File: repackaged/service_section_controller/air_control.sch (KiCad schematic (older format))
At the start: 18 parts

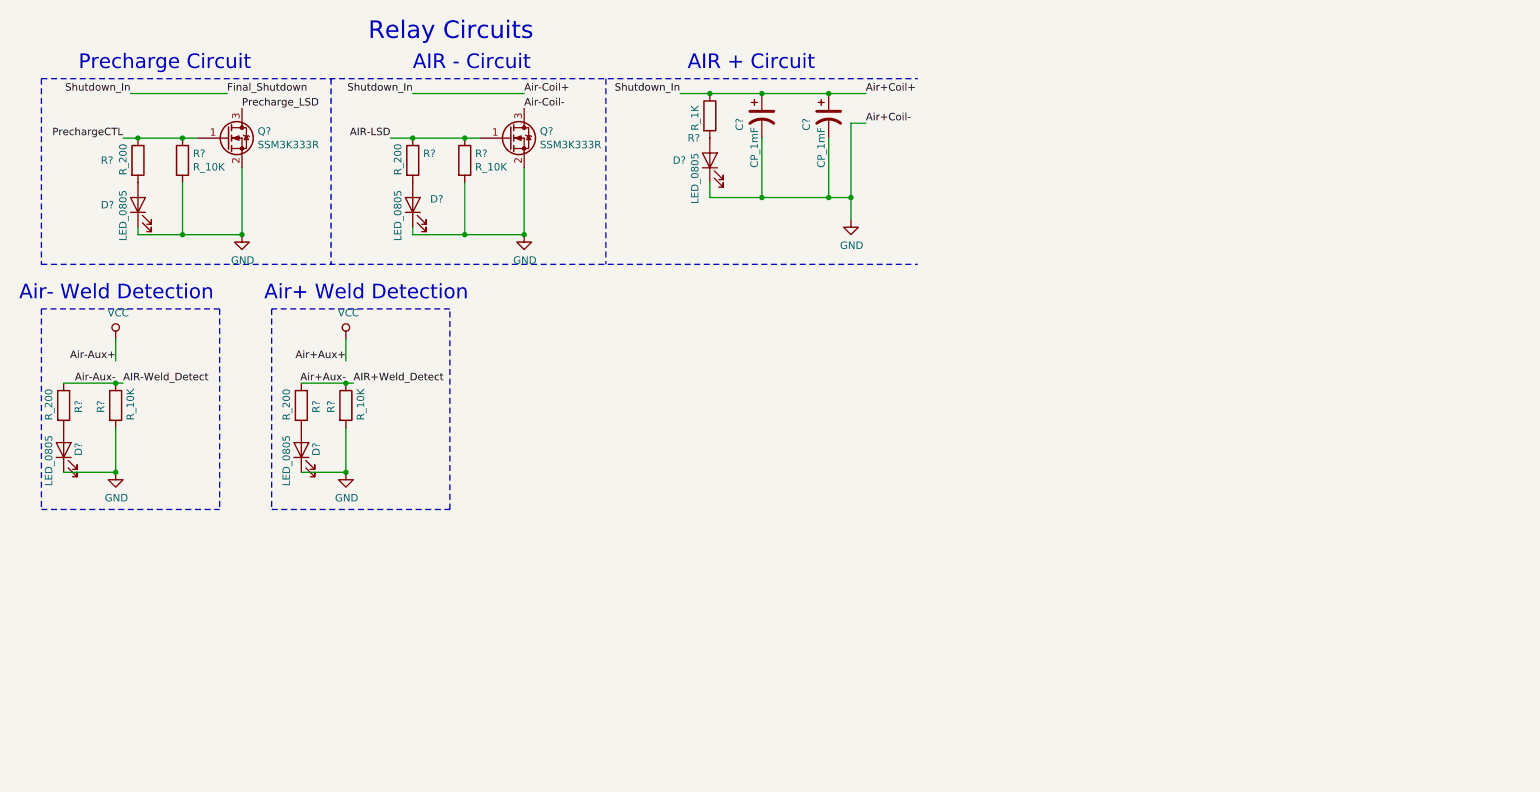
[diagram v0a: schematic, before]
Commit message: changed labels to global and added lin reg
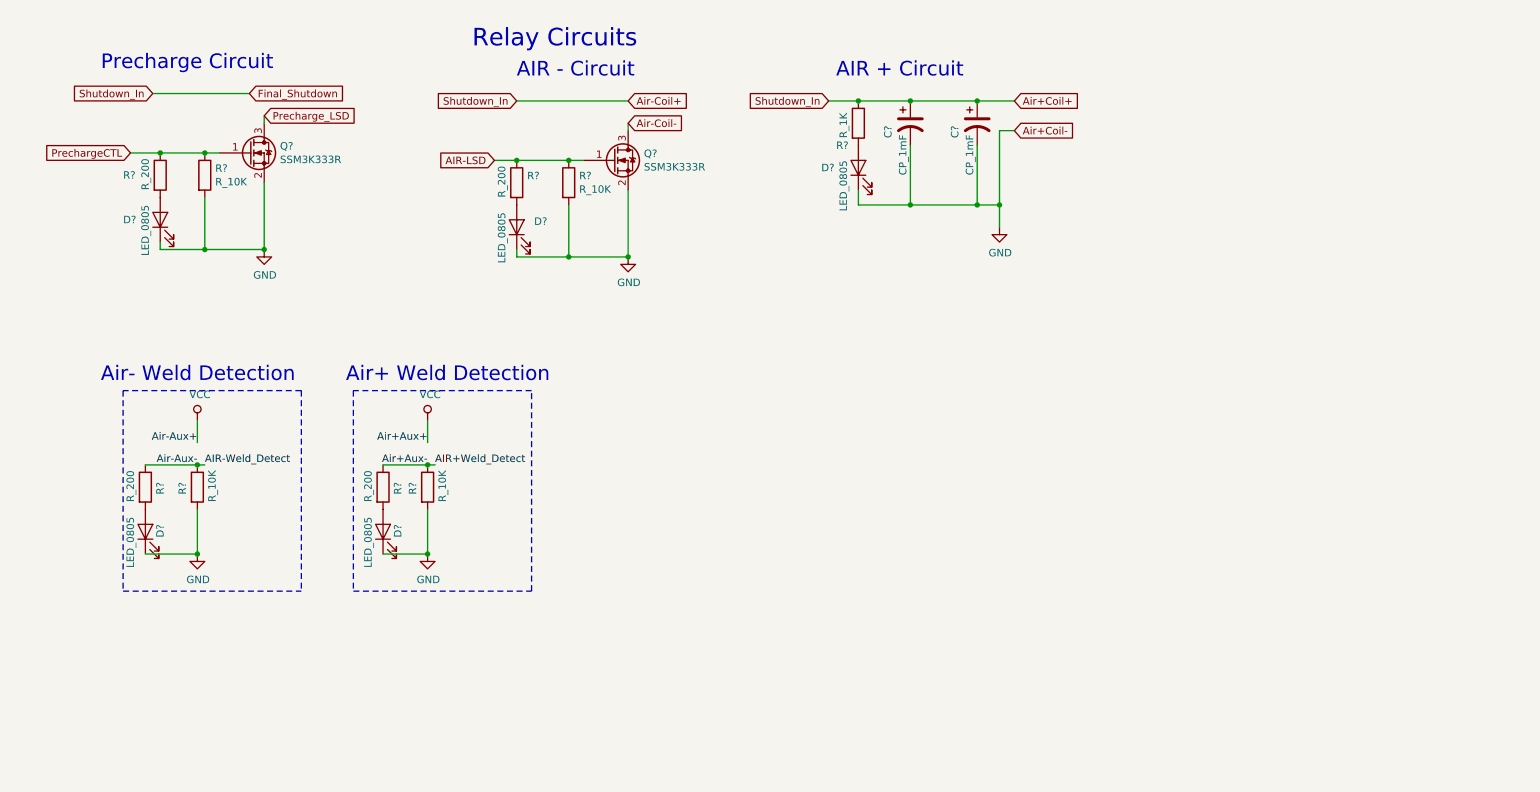
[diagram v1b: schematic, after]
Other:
- moved on the sheet: C?, D?, Q?, R?

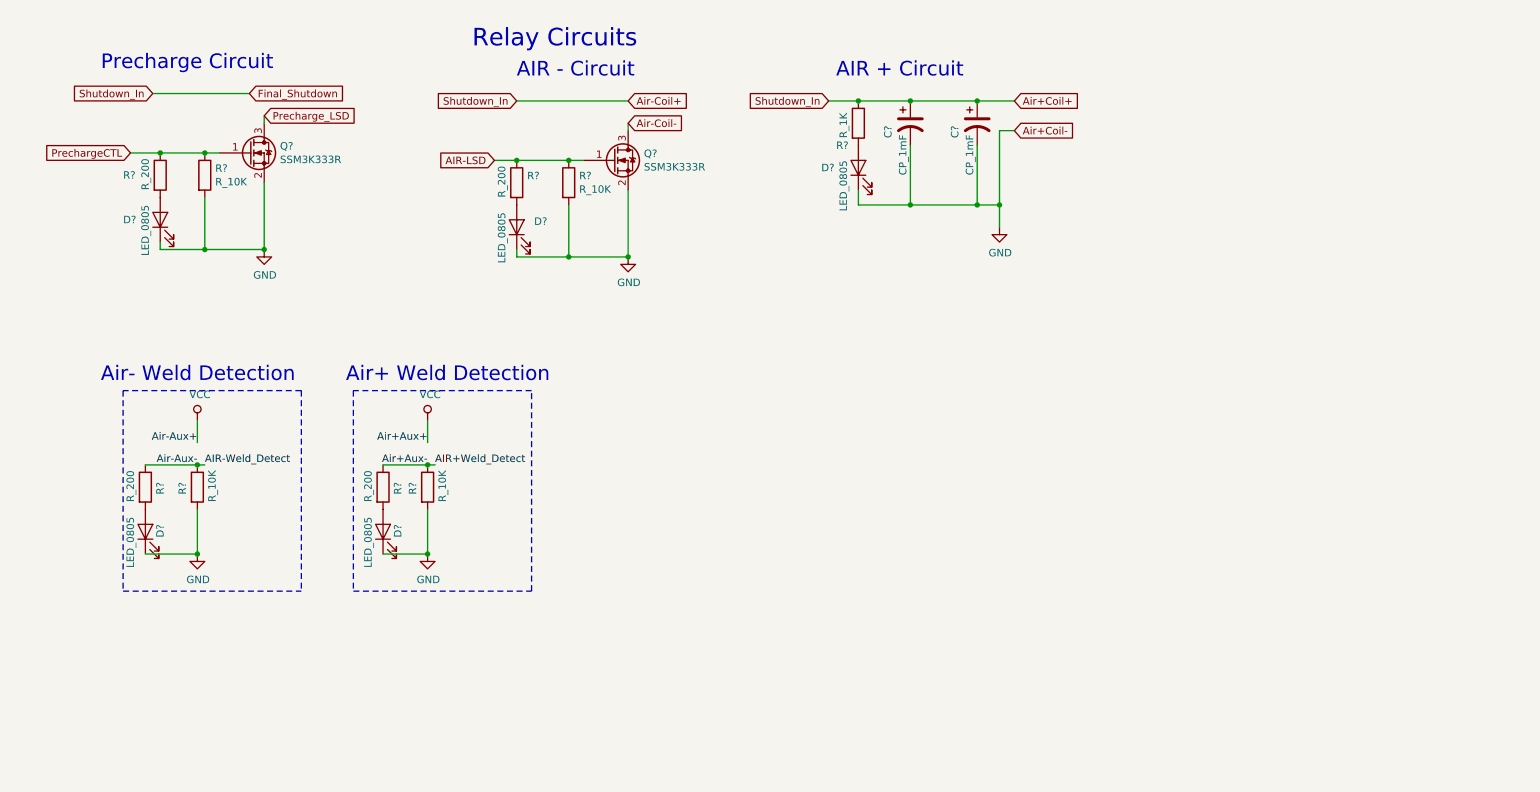
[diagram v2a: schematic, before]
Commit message: modify net labels for LSD circuits
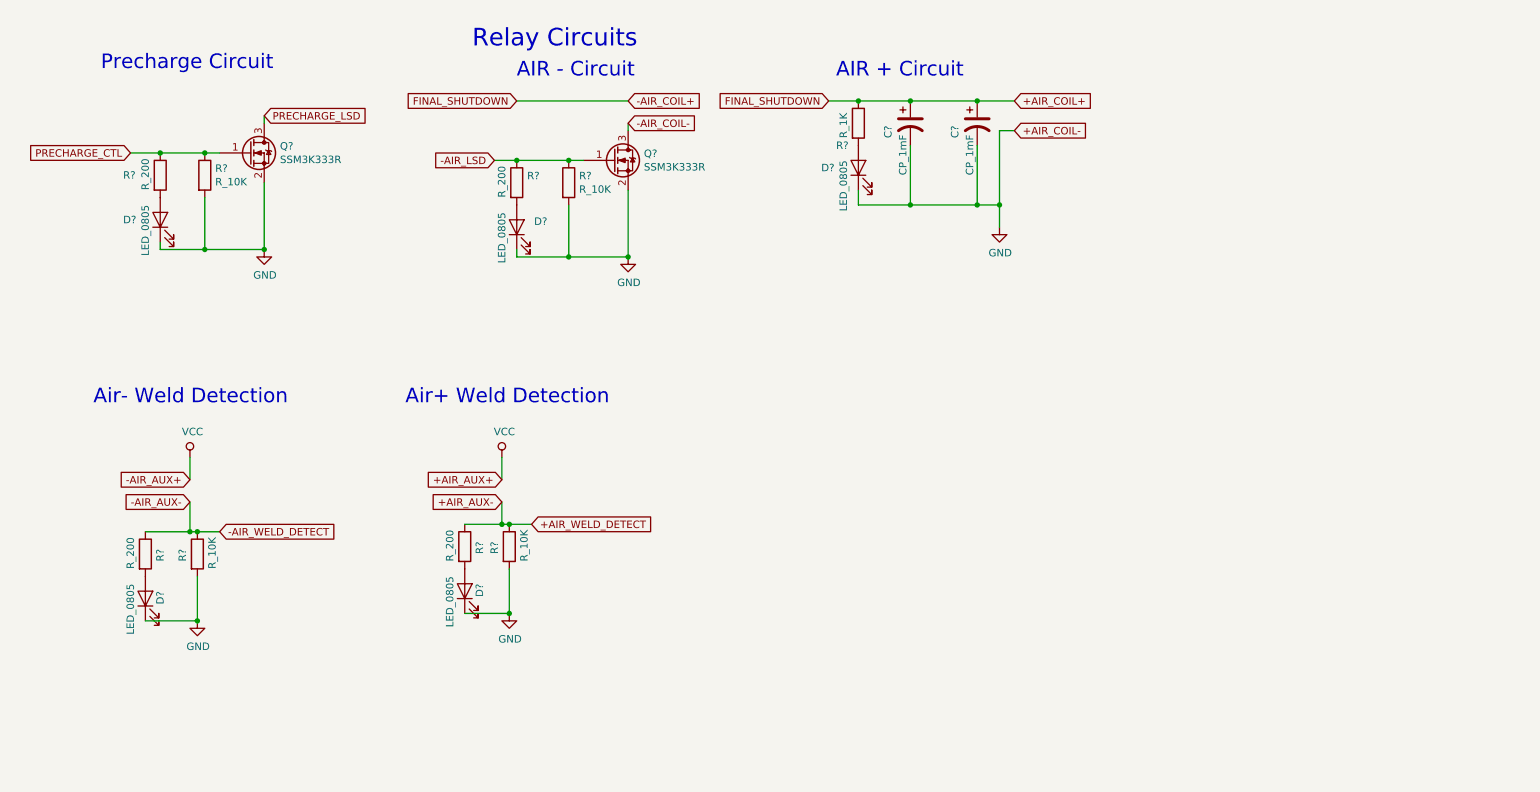
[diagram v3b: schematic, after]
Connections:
- net AIR+Weld_Detect renamed +AIR_AUX-
- net AIR-LSD renamed -AIR_LSD
- net AIR-Weld_Detect renamed -AIR_AUX-
- net Air+Coil+ renamed +AIR_COIL+
- net Air-Coil- renamed -AIR_COIL-
- net PrechargeCTL renamed PRECHARGE_CTL
- net Precharge_LSD renamed PRECHARGE_LSD
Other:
- moved on the sheet: D?, R?

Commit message: changed labels and power nets and added fusing
changed relevant labels to global labels and checked that the
naming is correct. Changed vcc nets to corresponding 5v or 12v.
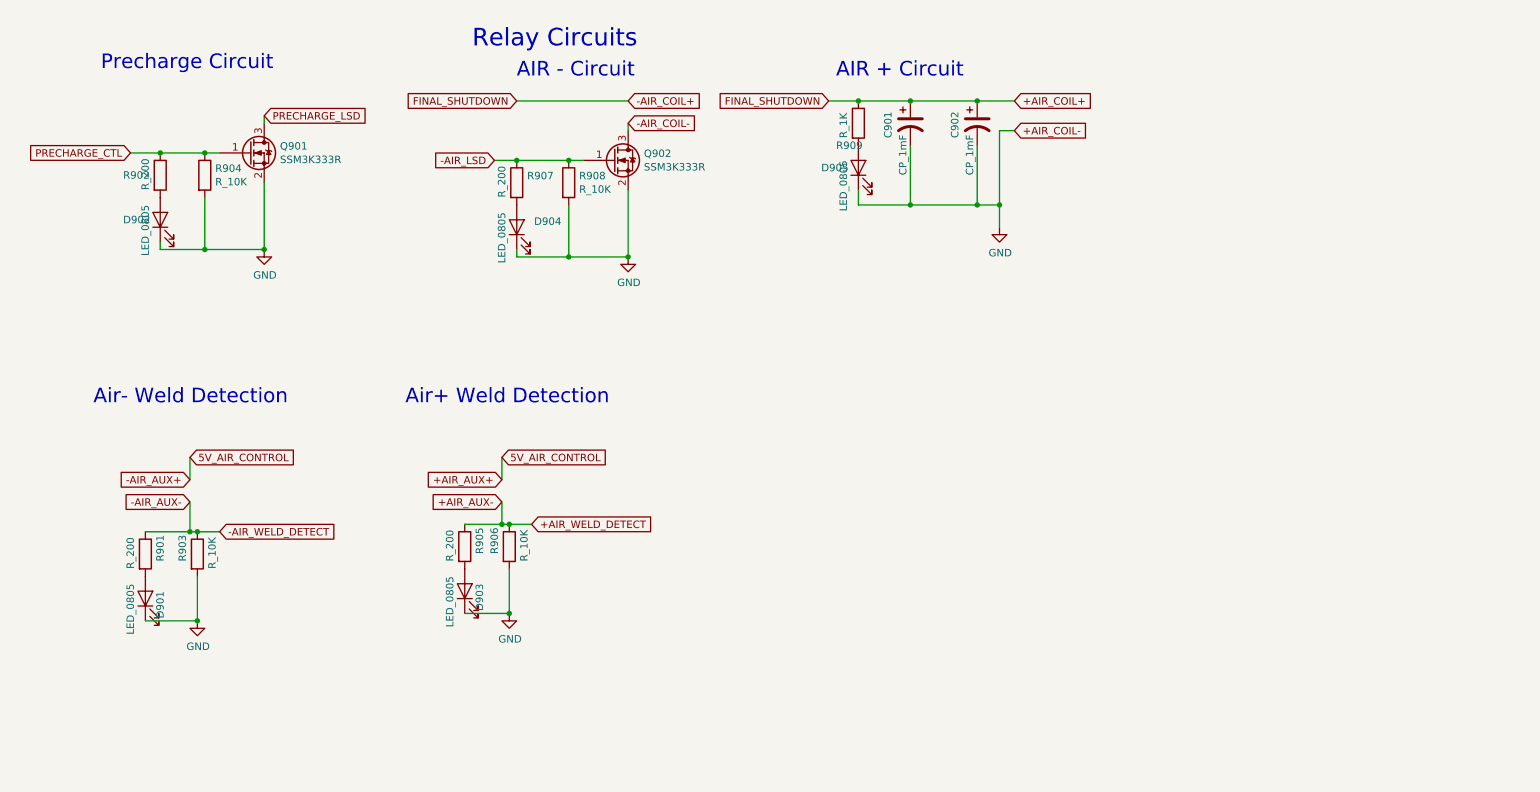
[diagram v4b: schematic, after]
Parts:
- gave numbers to parts that had none: 18
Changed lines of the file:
@@
 $EndComp
 $Comp
-L formula:R_10K R?
+L formula:R_10K R906
 U 1 1 61065F72
 P 4000 4200
-F 0 "R?" V 3900 4150 50  0000 L CNN
+F 0 "R906" V 3900 4150 50  0000 L CNN
 F 1 "R_10K" V 4100 4100 50  0000 L CNN
 F 2 "footprints:R_0805_OEM" H 3930 4200 50  0001 C CNN
@@
 $EndComp
 $Comp
-L formula:LED_0805 D?
+L formula:LED_0805 D903
 U 1 1 61065F7B
 P 3700 4500
-F 0 "D?" H 3750 4400 50  0000 R CNN
+F 0 "D903" H 3750 4400 50  0000 R CNN
 F 1 "LED_0805" H 3800 4600 50  0000 R CNN
 F 2 "footprints:LED_0805_OEM" H 3600 4500 50  0001 C CNN
@@
 $EndComp
 $Comp
-L formula:R_200 R?
+L formula:R_200 R905
 U 1 1 61065F84
 P 3700 4200
-F 0 "R?" V 3800 4150 50  0000 L CNN
+F 0 "R905" V 3800 4150 50  0000 L CNN
 F 1 "R_200" V 3600 4100 50  0000 L CNN
 F 2 "footprints:R_0805_OEM" H 3630 4200 50  0001 C CNN
@@
 Wire Wire Line
 	3950 3600 3950 3750
-$Comp
-L power:VCC #PWR0199
-U 1 1 61065F8F
-P 3950 3600
-F 0 "#PWR0199" H 3950 3450 50  0001 C CNN
-F 1 "VCC" H 3967 3773 50  0000 C CNN
-F 2 "" H 3950 3600 50  0001 C CNN
-F 3 "" H 3950 3600 50  0001 C CNN
-	1    3950 3600
-	1    0    0    -1
-$EndComp
 $Comp
 L power:GND #PWR0200
@@
 	1900 4400 1900 4700
 $Comp
-L formula:LED_0805 D?
+L formula:LED_0805 D901
 U 1 1 61065FA0
 P 1550 4550
-F 0 "D?" H 1600 4450 50  0000 R CNN
+F 0 "D901" H 1600 4450 50  0000 R CNN
 F 1 "LED_0805" H 1650 4650 50  0000 R CNN
 F 2 "footprints:LED_0805_OEM" H 1450 4550 50  0001 C CNN
@@
 	1550 4100 1850 4100
 $Comp
-L formula:R_200 R?
+L formula:R_200 R901
 U 1 1 61065FAA
 P 1550 4250
-F 0 "R?" V 1650 4200 50  0000 L CNN
+F 0 "R901" V 1650 4200 50  0000 L CNN
 F 1 "R_200" V 1450 4150 50  0000 L CNN
 F 2 "footprints:R_0805_OEM" H 1480 4250 50  0001 C CNN
@@
 $EndComp
 $Comp
-L formula:R_10K R?
+L formula:R_10K R903
 U 1 1 61065FB3
 P 1900 4250
-F 0 "R?" V 1800 4200 50  0000 L CNN
+F 0 "R903" V 1800 4200 50  0000 L CNN
 F 1 "R_10K" V 2000 4150 50  0000 L CNN
 F 2 "footprints:R_0805_OEM" H 1830 4250 50  0001 C CNN
@@
 Wire Wire Line
 	1850 3600 1850 3750
-$Comp
-L power:VCC #PWR0201
-U 1 1 61065FBC
-P 1850 3600
-F 0 "#PWR0201" H 1850 3450 50  0001 C CNN
-F 1 "VCC" H 1867 3773 50  0000 C CNN
-F 2 "" H 1850 3600 50  0001 C CNN
-F 3 "" H 1850 3600 50  0001 C CNN
-	1    1850 3600
-	1    0    0    -1
-$EndComp
 Text Notes 3300 3250 0    98   ~ 0
 Air+ Weld Detection
@@
 	4800 1800 4800 2250
 $Comp
-L formula:LED_0805 D?
+L formula:LED_0805 D904
 U 1 1 6106600B
 P 4050 2050
-F 0 "D?" V 4089 1933 50  0000 R CNN
+F 0 "D904" V 4089 1933 50  0000 R CNN
 F 1 "LED_0805" H 4150 2150 50  0000 R CNN
 F 2 "footprints:LED_0805_OEM" H 3950 2050 50  0001 C CNN
@@
 Connection ~ 4400 1600
 $Comp
-L formula:R_10K R?
+L formula:R_10K R908
 U 1 1 61066016
 P 4400 1750
-F 0 "R?" H 4470 1796 50  0000 L CNN
+F 0 "R908" H 4470 1796 50  0000 L CNN
 F 1 "R_10K" H 4470 1705 50  0000 L CNN
 F 2 "footprints:R_0805_OEM" H 4330 1750 50  0001 C CNN
@@
 Connection ~ 4050 1600
 $Comp
-L formula:R_200 R?
+L formula:R_200 R907
 U 1 1 61066021
 P 4050 1750
-F 0 "R?" H 4120 1796 50  0000 L CNN
+F 0 "R907" H 4120 1796 50  0000 L CNN
 F 1 "R_200" V 3950 1650 50  0000 L CNN
 F 2 "footprints:R_0805_OEM" H 3980 1750 50  0001 C CNN
@@
 	4500 1600 4400 1600
 $Comp
-L formula:SSM3K333R Q?
+L formula:SSM3K333R Q902
 U 1 1 6106602C
 P 4700 1600
-F 0 "Q?" H 4906 1646 50  0000 L CNN
+F 0 "Q902" H 4906 1646 50  0000 L CNN
 F 1 "SSM3K333R" H 4906 1555 50  0000 L CNN
 F 2 "footprints:SOT-23F" H 4900 1525 50  0001 L CIN
@@
 Connection ~ 1950 1550
 $Comp
-L formula:R_200 R?
+L formula:R_200 R902
 U 1 1 61066040
 P 1650 1700
-F 0 "R?" H 1400 1700 50  0000 L CNN
+F 0 "R902" H 1400 1700 50  0000 L CNN
 F 1 "R_200" V 1550 1600 50  0000 L CNN
 F 2 "footprints:R_0805_OEM" H 1580 1700 50  0001 C CNN
@@
 $EndComp
 $Comp
-L formula:LED_0805 D?
+L formula:LED_0805 D902
 U 1 1 61066049
 P 1650 2000
-F 0 "D?" V 1650 2250 50  0000 R CNN
+F 0 "D902" V 1650 2250 50  0000 R CNN
 F 1 "LED_0805" H 1750 2100 50  0000 R CNN
 F 2 "footprints:LED_0805_OEM" H 1550 2000 50  0001 C CNN
@@
 	2050 1550 1950 1550
 $Comp
-L formula:SSM3K333R Q?
+L formula:SSM3K333R Q901
 U 1 1 61066054
 P 2250 1550
-F 0 "Q?" H 2456 1596 50  0000 L CNN
+F 0 "Q901" H 2456 1596 50  0000 L CNN
 F 1 "SSM3K333R" H 2456 1505 50  0000 L CNN
 F 2 "footprints:SOT-23F" H 2450 1475 50  0001 L CIN
@@
 Air- Weld Detection
 $Comp
-L formula:R_10K R?
+L formula:R_10K R904
 U 1 1 61066090
 P 1950 1700
-F 0 "R?" H 2020 1746 50  0000 L CNN
+F 0 "R904" H 2020 1746 50  0000 L CNN
 F 1 "R_10K" H 2020 1655 50  0000 L CNN
 F 2 "footprints:R_0805_OEM" H 1880 1700 50  0001 C CNN
@@
 	6150 1200 6350 1200
 $Comp
-L formula:R_1K R?
+L formula:R_1K R909
 U 1 1 61065FF8
 P 6350 1350
-F 0 "R?" H 6200 1200 50  0000 L CNN
+F 0 "R909" H 6200 1200 50  0000 L CNN
 F 1 "R_1K" V 6250 1250 50  0000 L CNN
 F 2 "footprints:R_0805_OEM" H 6280 1350 50  0001 C CNN
@@
 	6350 1200 6700 1200
 $Comp
-L formula:CP_1mF C?
+L formula:CP_1mF C901
 U 1 1 61065FED
 P 6700 1350
-F 0 "C?" V 6550 1250 50  0000 L CNN
+F 0 "C901" V 6550 1250 50  0000 L CNN
 F 1 "CP_1mF" V 6650 1000 50  0000 L CNN
 F 2 "footprints:C_Radial_D10_L13_P5_OEM" H 6625 1350 50  0001 C CNN
@@
 	6700 1200 7150 1200
 $Comp
-L formula:CP_1mF C?
+L formula:CP_1mF C902
 U 1 1 61065FE1
 P 7150 1350
-F 0 "C?" V 7000 1250 50  0000 L CNN
+F 0 "C902" V 7000 1250 50  0000 L CNN
 F 1 "CP_1mF" V 7100 1000 50  0000 L CNN
 F 2 "footprints:C_Radial_D10_L13_P5_OEM" H 7075 1350 50  0001 C CNN
@@
 	7150 1200 7400 1200
 $Comp
-L formula:LED_0805 D?
+L formula:LED_0805 D905
 U 1 1 61065FD5
 P 6350 1650
-F 0 "D?" V 6350 1900 50  0000 R CNN
+F 0 "D905" V 6350 1900 50  0000 R CNN
 F 1 "LED_0805" H 6400 1750 50  0000 R CNN
 F 2 "footprints:LED_0805_OEM" H 6250 1650 50  0001 C CNN
@@
 Wire Wire Line
 	3950 4050 4000 4050
+Text GLabel 1850 3600 2    50   Input ~ 0
+5V_AIR_CONTROL
+Text GLabel 3950 3600 2    50   Input ~ 0
+5V_AIR_CONTROL
 $EndSCHEMATC

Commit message: updated schematic
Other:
- note added: "AIR CONTROL RELAY CIRCUITS"
- note removed: "Relay Circuits"
- moved on the sheet: C901, C902, D901, D902, D903, D904, D905, Q901, Q902, R901, R902, R903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
